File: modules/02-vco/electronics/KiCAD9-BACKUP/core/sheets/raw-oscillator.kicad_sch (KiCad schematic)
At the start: 56 parts, among them Q1 BC847BS, Q2 MMBT3906, Q3 J111, Q4 MMBFJ111, Q5 MMBT5551, U1 TL072, U2 TL072, U3 LM311

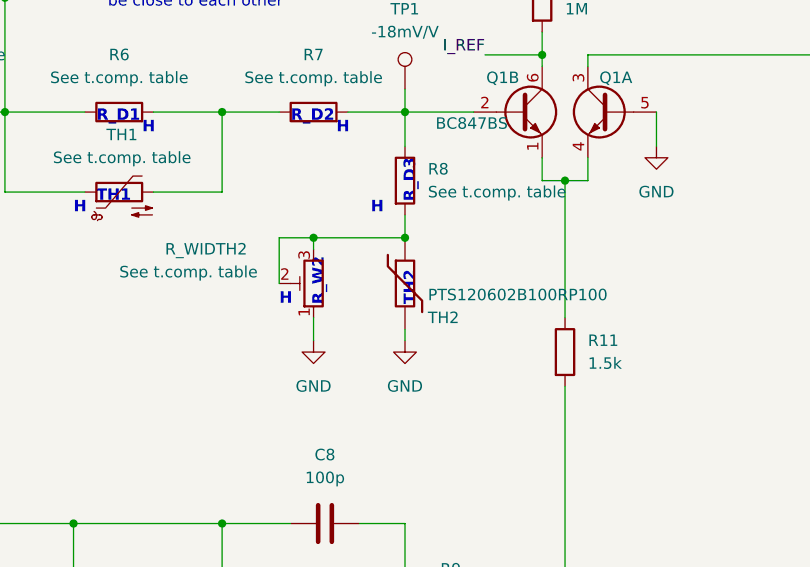
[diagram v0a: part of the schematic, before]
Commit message: Fix: Replace generic MMBT3906 with ON Semi for Q2
Q2 is the actuator in the master current servo loop (U1B → Q2) that sets the tail current for the exponential converter. The previous BOM specified the generic LCSC part C7420354, which JLCPCB silently substituted between production batches: batch 1 (Jan 2026) received a working part, while batches 2 and 3 received Zhuhai Hongjiacheng (R+O) MMBT3906 parts under the same C-code.

The R+O datasheet only characterizes hFE at IC = −10 mA and above, with no minimum specified at low collector currents. The circuit operates Q2 at sub-milliamp currents, where the substituted part has insufficient gain to close the servo loop. U1B saturates against the negative supply rail trying to compensate, leaving Q2's collector current stuck at a fixed (too-low) value regardless of CV input.
Symptoms across all affected boards (20+ units, fully uniform):

- VCO pitch ceiling at ~70 Hz
- Pitch plateaus and flattens above a certain CV — no further response to increasing CV
- R_BIAS1 trim has no effect on output (loop railed)
- TP1 floats at ~1V instead of being servoed to 0V
- U1B output pinned at −10.3V (TL072 negative rail)

Verified by swapping Q2 with a verified-genuine 2N3906 on two broken boards — both immediately tracked V/oct correctly across full CV range.
The replacement part ON Semi MMBT3906LT1G (LCSC C53444) explicitly specifies hFE ≥ 60 at IC = −0.1 mA in its datasheet, guaranteeing correct behavior in this circuit's operating range.
Changes:

BOM: Q2 LCSC part number changed from C7420354 → C53444
Schematic annotation updated to specify ON Semi MMBT3906LT1G
Production note added: "Q2 (C53444): Do not substitute. Must be ON Semi MMBT3906LT1G."
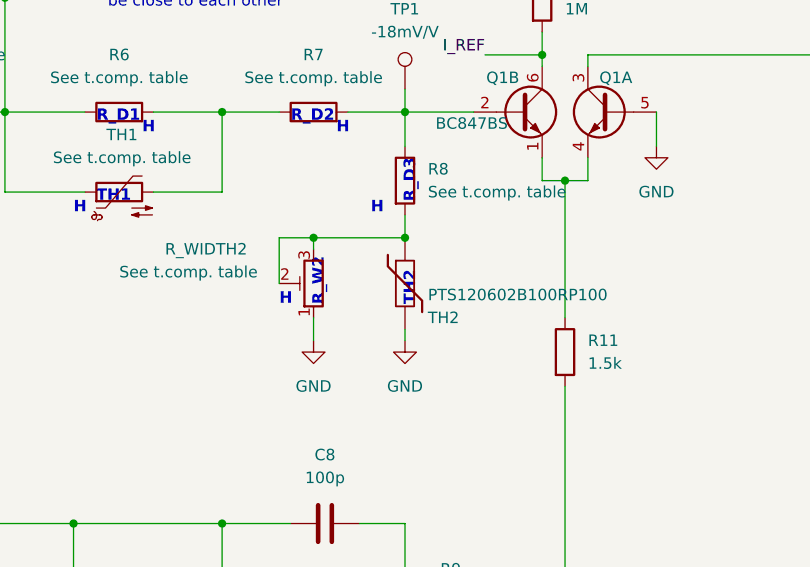
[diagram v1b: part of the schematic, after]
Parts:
- Q1: footprint Shmoergh_Custom_Footprints:SOT-363_SC-70-6 -> Package_TO_SOT_SMD:SOT-363_SC-70-6
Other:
- company: Shmøergh -> (none)
- title: Moduleur VCO core -> (none)
